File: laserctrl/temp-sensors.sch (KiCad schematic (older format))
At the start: 24 parts

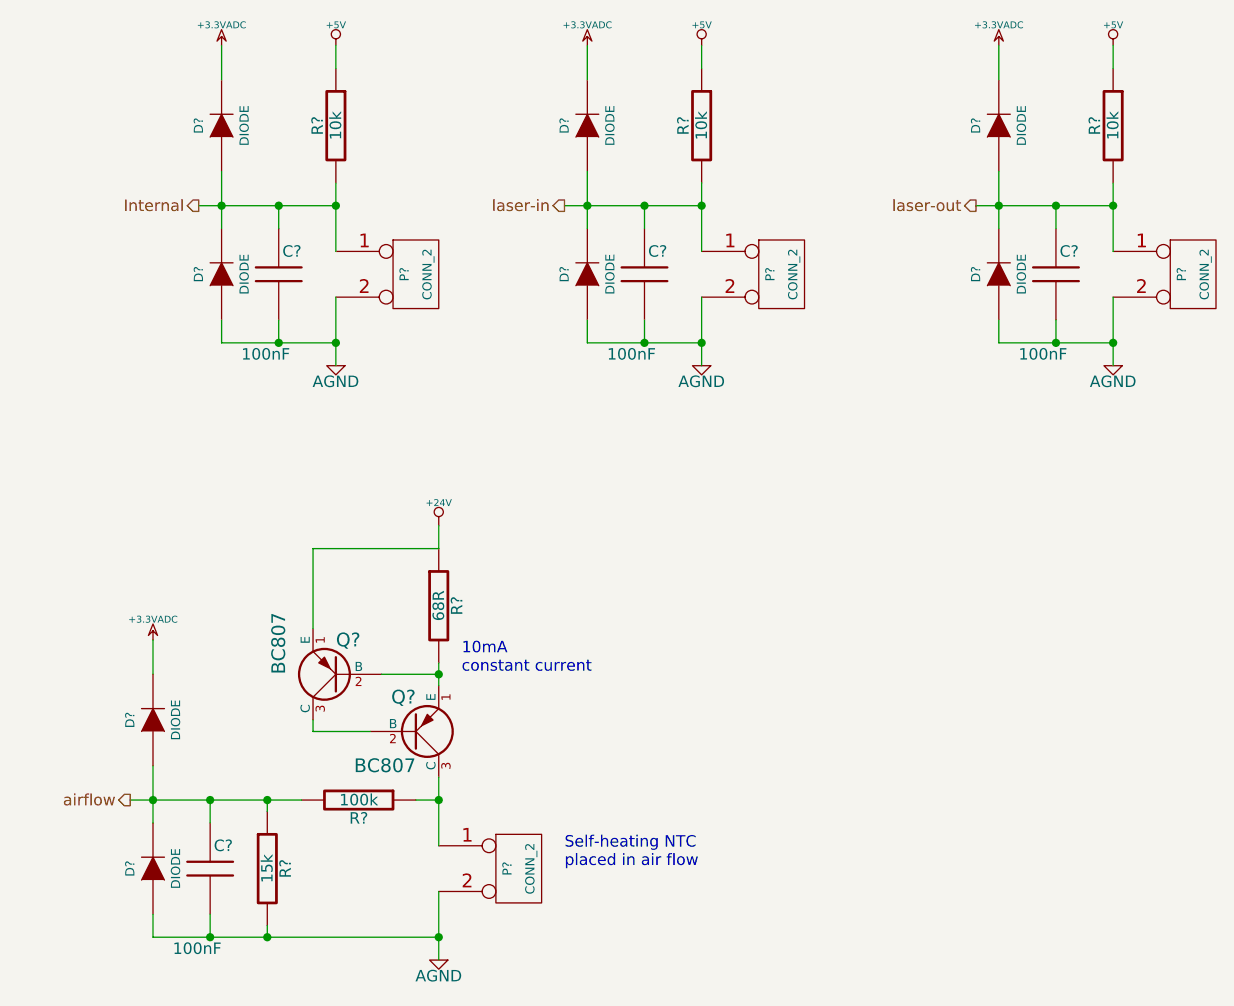
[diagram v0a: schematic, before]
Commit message: Added the chiller and the USB/Serial/ISP/SD subsystems and added some specs on the chiller protocol
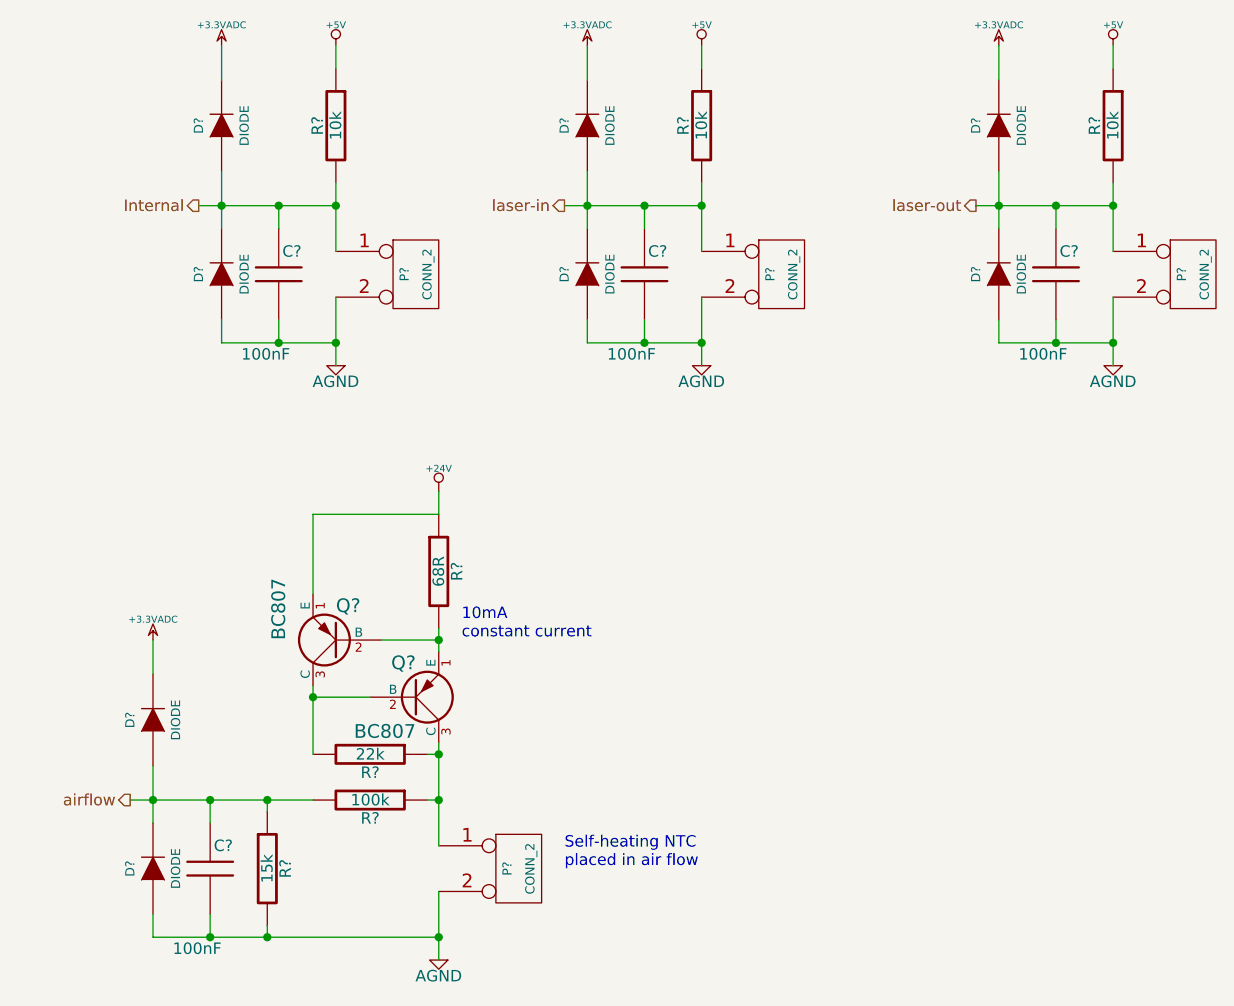
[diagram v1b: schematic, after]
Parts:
- added R?: 22k, symbol R
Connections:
- net at P?.1 (P1), Q?.3 (C), R?.1: now also R?.1
- net at Q?.2 (B), Q?.3 (C): now also R?.2
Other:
- moved on the sheet: Q?, R?
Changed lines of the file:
@@
-EESchema Schematic File Version 2  date 2011-11-05T15:41:06 CET
+EESchema Schematic File Version 2  date 2011-11-06T20:55:52 CET
 LIBS:power
 LIBS:device
@@
 $Descr A4 11700 8267
 encoding utf-8
-Sheet 2 9
+Sheet 4 11
 Title ""
-Date "5 nov 2011"
+Date "6 nov 2011"
 Rev ""
 Comp ""
@@
 Comment4 ""
 $EndDescr
+Connection ~ 2550 4200
+Wire Wire Line
+	2550 4150 2550 4600
+Wire Wire Line
+	2550 4200 2500 4200
+Connection ~ 2550 3700
+Wire Wire Line
+	2550 3650 2550 3750
+Wire Wire Line
+	2000 3500 2000 3150
+Wire Wire Line
+	2000 3150 2550 3150
+Connection ~ 1800 5000
+Wire Wire Line
+	1800 5000 1800 4950
+Connection ~ 1800 4400
+Wire Wire Line
+	1800 4400 1800 4450
+Wire Wire Line
+	2500 4400 2550 4400
+Wire Wire Line
+	1600 1100 1600 1250
+Connection ~ 1600 1800
+Wire Wire Line
+	2100 1100 2100 1200
+Wire Wire Line
+	2100 1700 2100 2000
+Connection ~ 1850 1800
+Wire Wire Line
+	1850 1800 1850 1900
+Wire Wire Line
+	1850 2300 1850 2400
+Wire Wire Line
+	1500 1800 2100 1800
+Connection ~ 2100 1800
+Wire Wire Line
+	2100 2500 2100 2200
+Connection ~ 2100 2400
+Wire Wire Line
+	1600 2300 1600 2400
+Wire Wire Line
+	1600 2400 2100 2400
+Connection ~ 1850 2400
+Wire Wire Line
+	1600 1900 1600 1650
+Wire Wire Line
+	3200 1900 3200 1650
+Connection ~ 3450 2400
+Wire Wire Line
+	3700 2400 3200 2400
+Wire Wire Line
+	3200 2400 3200 2300
+Connection ~ 3700 2400
+Wire Wire Line
+	3700 2500 3700 2200
+Connection ~ 3700 1800
+Wire Wire Line
+	3100 1800 3700 1800
+Wire Wire Line
+	3450 2400 3450 2300
+Wire Wire Line
+	3450 1900 3450 1800
+Connection ~ 3450 1800
+Wire Wire Line
+	3700 1700 3700 2000
+Wire Wire Line
+	3700 1100 3700 1200
+Connection ~ 3200 1800
+Wire Wire Line
+	3200 1100 3200 1250
+Wire Wire Line
+	5000 1100 5000 1250
+Connection ~ 5000 1800
+Wire Wire Line
+	5500 1100 5500 1200
+Wire Wire Line
+	5500 1700 5500 2000
+Connection ~ 5250 1800
+Wire Wire Line
+	5250 1800 5250 1900
+Wire Wire Line
+	5250 2300 5250 2400
+Wire Wire Line
+	4900 1800 5500 1800
+Connection ~ 5500 1800
+Wire Wire Line
+	5500 2500 5500 2200
+Connection ~ 5500 2400
+Wire Wire Line
+	5000 2300 5000 2400
+Wire Wire Line
+	5000 2400 5500 2400
+Connection ~ 5250 2400
+Wire Wire Line
+	5000 1900 5000 1650
+Wire Wire Line
+	1300 4500 1300 4250
+Connection ~ 1550 5000
+Wire Wire Line
+	1300 4900 1300 5000
+Connection ~ 2550 5000
+Wire Wire Line
+	2550 5100 2550 4800
+Connection ~ 2550 4400
+Wire Wire Line
+	1550 4900 1550 5000
+Wire Wire Line
+	1550 4400 1550 4500
+Connection ~ 1550 4400
+Connection ~ 1300 4400
+Wire Wire Line
+	1300 3700 1300 3850
+Wire Wire Line
+	1200 4400 2000 4400
+Wire Wire Line
+	1300 5000 2550 5000
+Wire Wire Line
+	2550 3150 2550 3050
+Wire Wire Line
+	2550 3700 2300 3700
+Wire Wire Line
+	2250 3950 2000 3950
+Wire Wire Line
+	2000 3900 2000 4200
+Connection ~ 2000 3950
+$Comp
+L R R?
+U 1 1 4EB5C802
+P 2250 4200
+F 0 "R?" V 2330 4200 50  0000 C CNN
+F 1 "22k" V 2250 4200 50  0000 C CNN
+	1    2250 4200
+	0    1    1    0
+$EndComp
 Text Notes 3100 4700 0    50   ~ 0
 Self-heating NTC\nplaced in air flow
-Text Notes 2650 3850 0    50   ~ 0
+Text Notes 2650 3700 0    50   ~ 0
 10mA\nconstant current
-Wire Wire Line
-	2000 4050 2000 4100
-Wire Wire Line
-	2000 4100 2250 4100
-Wire Wire Line
-	2550 3850 2300 3850
-Wire Wire Line
-	2550 3200 2550 3300
-Wire Wire Line
-	2550 5000 1300 5000
-Wire Wire Line
-	1950 4400 1200 4400
-Wire Wire Line
-	1300 3700 1300 3850
-Connection ~ 1300 4400
-Wire Wire Line
-	2550 4600 2550 4300
-Connection ~ 1550 4400
-Wire Wire Line
-	1550 4500 1550 4400
-Wire Wire Line
-	1550 5000 1550 4900
-Connection ~ 2550 4400
-Wire Wire Line
-	2550 4800 2550 5100
-Connection ~ 2550 5000
-Wire Wire Line
-	1300 5000 1300 4900
-Connection ~ 1550 5000
-Wire Wire Line
-	1300 4250 1300 4500
-Wire Wire Line
-	5000 1650 5000 1900
-Connection ~ 5250 2400
-Wire Wire Line
-	5500 2400 5000 2400
-Wire Wire Line
-	5000 2400 5000 2300
-Connection ~ 5500 2400
-Wire Wire Line
-	5500 2200 5500 2500
-Connection ~ 5500 1800
-Wire Wire Line
-	5500 1800 4900 1800
-Wire Wire Line
-	5250 2400 5250 2300
-Wire Wire Line
-	5250 1900 5250 1800
-Connection ~ 5250 1800
-Wire Wire Line
-	5500 2000 5500 1700
-Wire Wire Line
-	5500 1100 5500 1200
-Connection ~ 5000 1800
-Wire Wire Line
-	5000 1100 5000 1250
-Wire Wire Line
-	3200 1100 3200 1250
-Connection ~ 3200 1800
-Wire Wire Line
-	3700 1100 3700 1200
-Wire Wire Line
-	3700 2000 3700 1700
-Connection ~ 3450 1800
-Wire Wire Line
-	3450 1900 3450 1800
-Wire Wire Line
-	3450 2400 3450 2300
-Wire Wire Line
-	3700 1800 3100 1800
-Connection ~ 3700 1800
-Wire Wire Line
-	3700 2200 3700 2500
-Connection ~ 3700 2400
-Wire Wire Line
-	3200 2300 3200 2400
-Wire Wire Line
-	3200 2400 3700 2400
-Connection ~ 3450 2400
-Wire Wire Line
-	3200 1650 3200 1900
-Wire Wire Line
-	1600 1650 1600 1900
-Connection ~ 1850 2400
-Wire Wire Line
-	2100 2400 1600 2400
-Wire Wire Line
-	1600 2400 1600 2300
-Connection ~ 2100 2400
-Wire Wire Line
-	2100 2200 2100 2500
-Connection ~ 2100 1800
-Wire Wire Line
-	2100 1800 1500 1800
-Wire Wire Line
-	1850 2400 1850 2300
-Wire Wire Line
-	1850 1900 1850 1800
-Connection ~ 1850 1800
-Wire Wire Line
-	2100 2000 2100 1700
-Wire Wire Line
-	2100 1100 2100 1200
-Connection ~ 1600 1800
-Wire Wire Line
-	1600 1100 1600 1250
-Wire Wire Line
-	2550 4400 2450 4400
-Wire Wire Line
-	1800 4450 1800 4400
-Connection ~ 1800 4400
-Wire Wire Line
-	1800 4950 1800 5000
-Connection ~ 1800 5000
-Wire Wire Line
-	2550 3300 2000 3300
-Wire Wire Line
-	2000 3300 2000 3650
-Wire Wire Line
-	2550 3900 2550 3800
-Connection ~ 2550 3850
 $Comp
 L +24V #PWR?
 U 1 1 4EB542F9
-P 2550 3200
-F 0 "#PWR?" H 2550 3150 20  0001 C CNN
-F 1 "+24V" H 2550 3300 30  0000 C CNN
-	1    2550 3200
+P 2550 3050
+F 0 "#PWR?" H 2550 3000 20  0001 C CNN
+F 1 "+24V" H 2550 3150 30  0000 C CNN
+	1    2550 3050
 	1    0    0    -1
 $EndComp
@@
 L R R?
 U 1 1 4EB542D5
-P 2550 3550
-F 0 "R?" V 2630 3550 50  0000 C CNN
-F 1 "68R" V 2550 3550 50  0000 C CNN
-	1    2550 3550
+P 2550 3400
+F 0 "R?" V 2630 3400 50  0000 C CNN
+F 1 "68R" V 2550 3400 50  0000 C CNN
+	1    2550 3400
 	1    0    0    -1
 $EndComp
@@
 L PNP Q?
 U 1 1 4EB542BA
-P 2100 3850
-F 0 "Q?" H 2100 3700 60  0000 R CNN
-F 1 "BC807" V 2350 3850 60  0000 R CNN
-	1    2100 3850
+P 2100 3700
+F 0 "Q?" H 2100 3550 60  0000 R CNN
+F 1 "BC807" V 2350 3700 60  0000 R CNN
+	1    2100 3700
 	-1   0    0    1
 $EndComp
@@
 L PNP Q?
 U 1 1 4EB542A8
-P 2450 4100
-F 0 "Q?" H 2450 3950 60  0000 R CNN
-F 1 "BC807" H 2450 4250 60  0000 R CNN
-	1    2450 4100
+P 2450 3950
+F 0 "Q?" H 2450 3800 60  0000 R CNN
+F 1 "BC807" H 2450 4100 60  0000 R CNN
+	1    2450 3950
 	1    0    0    1
 $EndComp
@@
 L R R?
 U 1 1 4EB528F0
-P 2200 4400
-F 0 "R?" V 2280 4400 50  0000 C CNN
-F 1 "100k" V 2200 4400 50  0000 C CNN
-	1    2200 4400
+P 2250 4400
+F 0 "R?" V 2330 4400 50  0000 C CNN
+F 1 "100k" V 2250 4400 50  0000 C CNN
+	1    2250 4400
 	0    1    1    0
 $EndComp

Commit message: Added a todo list so I don't forget the last bits and tried annotating different ways
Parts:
- gave numbers to parts that had none: 25
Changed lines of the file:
@@
-EESchema Schematic File Version 2  date 2011-11-06T20:55:52 CET
+EESchema Schematic File Version 2  date 2011-11-06T22:48:15 CET
 LIBS:power
 LIBS:device
@@
 Connection ~ 2000 3950
 $Comp
-L R R?
+L R R19
 U 1 1 4EB5C802
 P 2250 4200
-F 0 "R?" V 2330 4200 50  0000 C CNN
+F 0 "R19" V 2330 4200 50  0000 C CNN
 F 1 "22k" V 2250 4200 50  0000 C CNN
 	1    2250 4200
@@
 10mA\nconstant current
 $Comp
-L +24V #PWR?
+L +24V #PWR36
 U 1 1 4EB542F9
 P 2550 3050
-F 0 "#PWR?" H 2550 3000 20  0001 C CNN
+F 0 "#PWR36" H 2550 3000 20  0001 C CNN
 F 1 "+24V" H 2550 3150 30  0000 C CNN
 	1    2550 3050
@@
 $EndComp
 $Comp
-L R R?
+L R R18
 U 1 1 4EB542D5
 P 2550 3400
-F 0 "R?" V 2630 3400 50  0000 C CNN
+F 0 "R18" V 2630 3400 50  0000 C CNN
 F 1 "68R" V 2550 3400 50  0000 C CNN
 	1    2550 3400
@@
 $EndComp
 $Comp
-L PNP Q?
+L PNP Q2
 U 1 1 4EB542BA
 P 2100 3700
-F 0 "Q?" H 2100 3550 60  0000 R CNN
+F 0 "Q2" H 2100 3550 60  0000 R CNN
 F 1 "BC807" V 2350 3700 60  0000 R CNN
 	1    2100 3700
@@
 $EndComp
 $Comp
-L PNP Q?
+L PNP Q3
 U 1 1 4EB542A8
 P 2450 3950
-F 0 "Q?" H 2450 3800 60  0000 R CNN
+F 0 "Q3" H 2450 3800 60  0000 R CNN
 F 1 "BC807" H 2450 4100 60  0000 R CNN
 	1    2450 3950
@@
 $EndComp
 $Comp
-L R R?
+L R R20
 U 1 1 4EB528F0
 P 2250 4400
-F 0 "R?" V 2330 4400 50  0000 C CNN
+F 0 "R20" V 2330 4400 50  0000 C CNN
 F 1 "100k" V 2250 4400 50  0000 C CNN
 	1    2250 4400
@@
 $EndComp
 $Comp
-L R R?
+L R R21
 U 1 1 4EB528C5
 P 1800 4700
-F 0 "R?" V 1880 4700 50  0000 C CNN
+F 0 "R21" V 1880 4700 50  0000 C CNN
 F 1 "15k" V 1800 4700 50  0000 C CNN
 	1    1800 4700
@@
 $EndComp
 $Comp
-L C C?
+L C C12
 U 1 1 4EB5260C
 P 1550 4700
-F 0 "C?" H 1450 4800 50  0000 L CNN
+F 0 "C12" H 1450 4800 50  0000 L CNN
 F 1 "100nF" H 1500 4350 50  0000 L CNN
 	1    1550 4700
@@
 $EndComp
 $Comp
-L AGND #PWR?
+L AGND #PWR38
 U 1 1 4EB5260B
 P 2550 5100
-F 0 "#PWR?" H 2550 5100 40  0001 C CNN
+F 0 "#PWR38" H 2550 5100 40  0001 C CNN
 F 1 "AGND" H 2550 5030 50  0000 C CNN
 	1    2550 5100
@@
 airflow
 $Comp
-L CONN_2 P?
+L CONN_2 P7
 U 1 1 4EB5260A
 P 2900 4700
-F 0 "P?" V 2850 4700 40  0000 C CNN
+F 0 "P7" V 2850 4700 40  0000 C CNN
 F 1 "CONN_2" V 2950 4700 40  0000 C CNN
 	1    2900 4700
@@
 $EndComp
 $Comp
-L DIODE D?
+L DIODE D8
 U 1 1 4EB52608
 P 1300 4050
-F 0 "D?" H 1300 4150 40  0000 C CNN
+F 0 "D8" H 1300 4150 40  0000 C CNN
 F 1 "DIODE" H 1300 3950 40  0000 C CNN
 	1    1300 4050
@@
 $EndComp
 $Comp
-L DIODE D?
+L DIODE D9
 U 1 1 4EB52607
 P 1300 4700
-F 0 "D?" H 1300 4800 40  0000 C CNN
+F 0 "D9" H 1300 4800 40  0000 C CNN
 F 1 "DIODE" H 1300 4600 40  0000 C CNN
 	1    1300 4700
@@
 $EndComp
 $Comp
-L +3.3VADC #PWR?
+L +3.3VADC #PWR37
 U 1 1 4EB52606
 P 1300 3700
-F 0 "#PWR?" H 1300 3820 20  0001 C CNN
+F 0 "#PWR37" H 1300 3820 20  0001 C CNN
 F 1 "+3.3VADC" H 1300 3790 30  0000 C CNN
 	1    1300 3700
@@
 $EndComp
 $Comp
-L +3.3VADC #PWR?
+L +3.3VADC #PWR31
 U 1 1 4EB52599
 P 5000 1100
-F 0 "#PWR?" H 5000 1220 20  0001 C CNN
+F 0 "#PWR31" H 5000 1220 20  0001 C CNN
 F 1 "+3.3VADC" H 5000 1190 30  0000 C CNN
 	1    5000 1100
@@
 $EndComp
 $Comp
-L DIODE D?
+L DIODE D7
 U 1 1 4EB52598
 P 5000 2100
-F 0 "D?" H 5000 2200 40  0000 C CNN
+F 0 "D7" H 5000 2200 40  0000 C CNN
 F 1 "DIODE" H 5000 2000 40  0000 C CNN
 	1    5000 2100
@@
 $EndComp
 $Comp
-L DIODE D?
+L DIODE D4
 U 1 1 4EB52597
 P 5000 1450
-F 0 "D?" H 5000 1550 40  0000 C CNN
+F 0 "D4" H 5000 1550 40  0000 C CNN
 F 1 "DIODE" H 5000 1350 40  0000 C CNN
 	1    5000 1450
@@
 $EndComp
 $Comp
-L +5V #PWR?
+L +5V #PWR32
 U 1 1 4EB52596
 P 5500 1100
-F 0 "#PWR?" H 5500 1190 20  0001 C CNN
+F 0 "#PWR32" H 5500 1190 20  0001 C CNN
 F 1 "+5V" H 5500 1190 30  0000 C CNN
 	1    5500 1100
@@
 $EndComp
 $Comp
-L CONN_2 P?
+L CONN_2 P6
 U 1 1 4EB52595
 P 5850 2100
-F 0 "P?" V 5800 2100 40  0000 C CNN
+F 0 "P6" V 5800 2100 40  0000 C CNN
 F 1 "CONN_2" V 5900 2100 40  0000 C CNN
 	1    5850 2100
@@
 laser-out
 $Comp
-L AGND #PWR?
+L AGND #PWR35
 U 1 1 4EB52594
 P 5500 2500
-F 0 "#PWR?" H 5500 2500 40  0001 C CNN
+F 0 "#PWR35" H 5500 2500 40  0001 C CNN
 F 1 "AGND" H 5500 2430 50  0000 C CNN
 	1    5500 2500
@@
 $EndComp
 $Comp
-L C C?
+L C C11
 U 1 1 4EB52593
 P 5250 2100
-F 0 "C?" H 5150 2200 50  0000 L CNN
+F 0 "C11" H 5150 2200 50  0000 L CNN
 F 1 "100nF" H 5200 1750 50  0000 L CNN
 	1    5250 2100
@@
 $EndComp
 $Comp
-L R R?
+L R R17
 U 1 1 4EB52592
 P 5500 1450
-F 0 "R?" V 5580 1450 50  0000 C CNN
+F 0 "R17" V 5580 1450 50  0000 C CNN
 F 1 "10k" V 5500 1450 50  0000 C CNN
 	1    5500 1450
@@
 $EndComp
 $Comp
-L R R?
+L R R16
 U 1 1 4EB52540
 P 3700 1450
-F 0 "R?" V 3780 1450 50  0000 C CNN
+F 0 "R16" V 3780 1450 50  0000 C CNN
 F 1 "10k" V 3700 1450 50  0000 C CNN
 	1    3700 1450
@@
 $EndComp
 $Comp
-L C C?
+L C C10
 U 1 1 4EB5253F
 P 3450 2100
-F 0 "C?" H 3350 2200 50  0000 L CNN
+F 0 "C10" H 3350 2200 50  0000 L CNN
 F 1 "100nF" H 3400 1750 50  0000 L CNN
 	1    3450 2100
@@
 $EndComp
 $Comp
-L AGND #PWR?
+L AGND #PWR34
 U 1 1 4EB5253E
 P 3700 2500
-F 0 "#PWR?" H 3700 2500 40  0001 C CNN
+F 0 "#PWR34" H 3700 2500 40  0001 C CNN
 F 1 "AGND" H 3700 2430 50  0000 C CNN
 	1    3700 2500
@@
 laser-in
 $Comp
-L CONN_2 P?
+L CONN_2 P5
 U 1 1 4EB5253D
 P 4050 2100
-F 0 "P?" V 4000 2100 40  0000 C CNN
+F 0 "P5" V 4000 2100 40  0000 C CNN
 F 1 "CONN_2" V 4100 2100 40  0000 C CNN
 	1    4050 2100
@@
 $EndComp
 $Comp
-L +5V #PWR?
+L +5V #PWR30
 U 1 1 4EB5253C
 P 3700 1100
-F 0 "#PWR?" H 3700 1190 20  0001 C CNN
+F 0 "#PWR30" H 3700 1190 20  0001 C CNN
 F 1 "+5V" H 3700 1190 30  0000 C CNN
 	1    3700 1100
@@
 $EndComp
 $Comp
-L DIODE D?
+L DIODE D3
 U 1 1 4EB5253B
 P 3200 1450
-F 0 "D?" H 3200 1550 40  0000 C CNN
+F 0 "D3" H 3200 1550 40  0000 C CNN
 F 1 "DIODE" H 3200 1350 40  0000 C CNN
 	1    3200 1450
@@
 $EndComp
 $Comp
-L DIODE D?
+L DIODE D6
 U 1 1 4EB5253A
 P 3200 2100
-F 0 "D?" H 3200 2200 40  0000 C CNN
+F 0 "D6" H 3200 2200 40  0000 C CNN
 F 1 "DIODE" H 3200 2000 40  0000 C CNN
 	1    3200 2100
@@
 $EndComp
 $Comp
-L +3.3VADC #PWR?
+L +3.3VADC #PWR29
 U 1 1 4EB52539
 P 3200 1100
-F 0 "#PWR?" H 3200 1220 20  0001 C CNN
+F 0 "#PWR29" H 3200 1220 20  0001 C CNN
 F 1 "+3.3VADC" H 3200 1190 30  0000 C CNN
 	1    3200 1100
@@
 $EndComp
 $Comp
-L +3.3VADC #PWR?
+L +3.3VADC #PWR27
 U 1 1 4EB52427
 P 1600 1100
-F 0 "#PWR?" H 1600 1220 20  0001 C CNN
+F 0 "#PWR27" H 1600 1220 20  0001 C CNN
 F 1 "+3.3VADC" H 1600 1190 30  0000 C CNN
 	1    1600 1100
@@
 $EndComp
 $Comp
-L DIODE D?
+L DIODE D5
 U 1 1 4EB52405
 P 1600 2100
-F 0 "D?" H 1600 2200 40  0000 C CNN
+F 0 "D5" H 1600 2200 40  0000 C CNN
 F 1 "DIODE" H 1600 2000 40  0000 C CNN
 	1    1600 2100
@@
 $EndComp
 $Comp
-L DIODE D?
+L DIODE D2
 U 1 1 4EB523F4
 P 1600 1450
-F 0 "D?" H 1600 1550 40  0000 C CNN
+F 0 "D2" H 1600 1550 40  0000 C CNN
 F 1 "DIODE" H 1600 1350 40  0000 C CNN
 	1    1600 1450
@@
 $EndComp
 $Comp
-L +5V #PWR?
+L +5V #PWR28
 U 1 1 4EB523C5
 P 2100 1100
-F 0 "#PWR?" H 2100 1190 20  0001 C CNN
+F 0 "#PWR28" H 2100 1190 20  0001 C CNN
 F 1 "+5V" H 2100 1190 30  0000 C CNN
 	1    2100 1100
@@
 $EndComp
 $Comp
-L CONN_2 P?
+L CONN_2 P4
 U 1 1 4EB523A3
 P 2450 2100
-F 0 "P?" V 2400 2100 40  0000 C CNN
+F 0 "P4" V 2400 2100 40  0000 C CNN
 F 1 "CONN_2" V 2500 2100 40  0000 C CNN
 	1    2450 2100
@@
 Internal
 $Comp
-L AGND #PWR?
+L AGND #PWR33
 U 1 1 4EB472F1
 P 2100 2500
-F 0 "#PWR?" H 2100 2500 40  0001 C CNN
+F 0 "#PWR33" H 2100 2500 40  0001 C CNN
 F 1 "AGND" H 2100 2430 50  0000 C CNN
 	1    2100 2500
@@
 $EndComp
 $Comp
-L C C?
+L C C9
 U 1 1 4EB46A9D
 P 1850 2100
-F 0 "C?" H 1750 2200 50  0000 L CNN
+F 0 "C9" H 1750 2200 50  0000 L CNN
 F 1 "100nF" H 1800 1750 50  0000 L CNN
 	1    1850 2100
@@
 $EndComp
 $Comp
-L R R?
+L R R15
 U 1 1 4EB46A84
 P 2100 1450
-F 0 "R?" V 2180 1450 50  0000 C CNN
+F 0 "R15" V 2180 1450 50  0000 C CNN
 F 1 "10k" V 2100 1450 50  0000 C CNN
 	1    2100 1450
